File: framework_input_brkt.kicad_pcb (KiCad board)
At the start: 2 copper layers, 18 x 9.5 mm, 8 parts, among them J1 FPR_LED, J2 fpc_input_conn, J3 PWRSW, J4 USB, J5 KnC

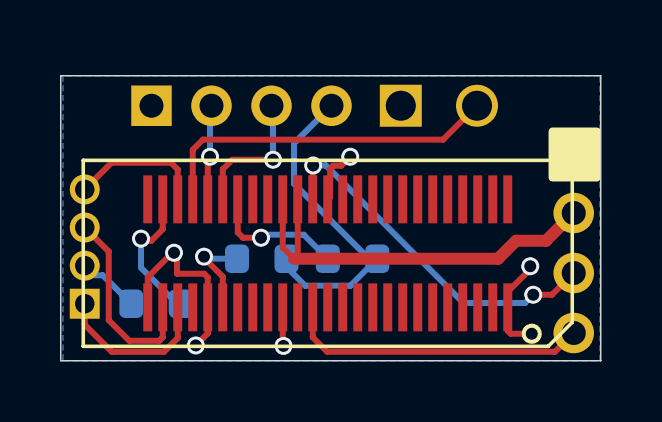
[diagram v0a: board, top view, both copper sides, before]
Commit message: Keep more of original design, only move the central through holes
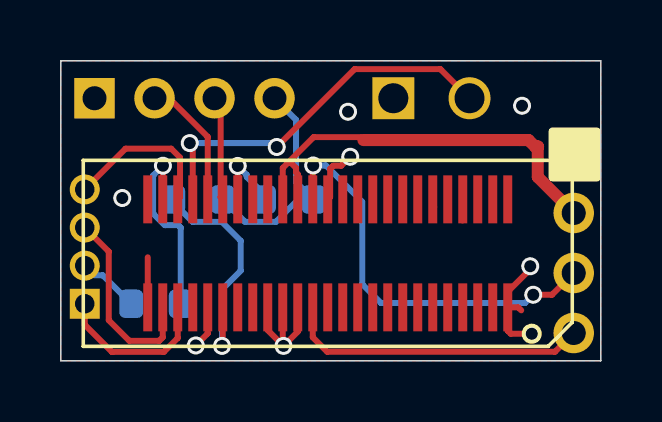
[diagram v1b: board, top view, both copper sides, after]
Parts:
- moved R1 2.90 mm to (153.2, 98.6)
- moved R2 2.90 mm to (150.2, 98.6)
- moved J4 1.92 mm to (146.8, 95.2)
- moved J3 0.35 mm to (156.7, 95.2)
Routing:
- net /KBL_P: track 14.1 -> 20.2 mm
- net /5VALW: track 3.10 -> 7.94 mm
- net Net-(J4-Pad4): track 10.6 -> 7.56 mm
- net /5VS: track 4.55 -> 2.59 mm
- net /FPR_LED_COM_5V: track 4.75 -> 6.50 mm
- net /CAPS_N: track 12.1 -> 13.7 mm
- net /USB_P: track 3.17 -> 4.39 mm, vias 1 -> 0
- net /USB_N: track 4.63 -> 3.48 mm, vias 1 -> 0
- net /SWITCH: track 11.7 -> 12.8 mm, vias 0 -> 2
- net /FPR_LED_W: track 4.56 -> 5.29 mm
- net GND: track 13.0 -> 13.1 mm, vias 6 -> 8
- added copper zone on F.Cu, net GND
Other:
- board size 18 x 9.5 mm -> 18 x 10 mm
- board text added: "5V"
- board text added: "FrmW input shim v3.2"
- board text added: "mobo edge"
- board text removed: "5v"
- board text removed: "FrmW input shim v3.1"
